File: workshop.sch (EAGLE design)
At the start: 8 parts, among them IC1 LM555N

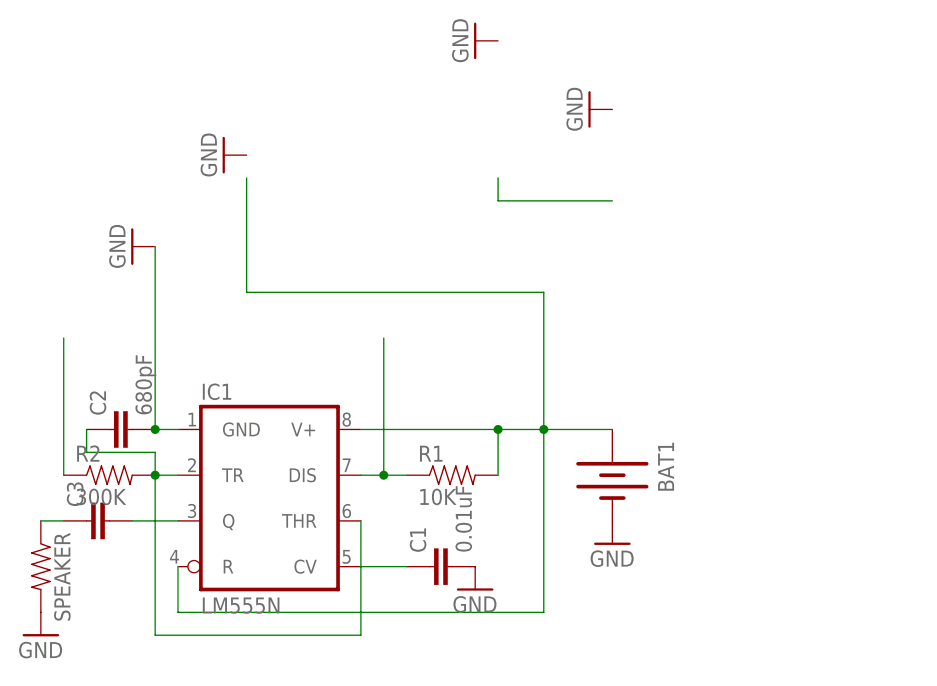
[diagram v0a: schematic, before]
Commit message: Simpler version with LED and switch
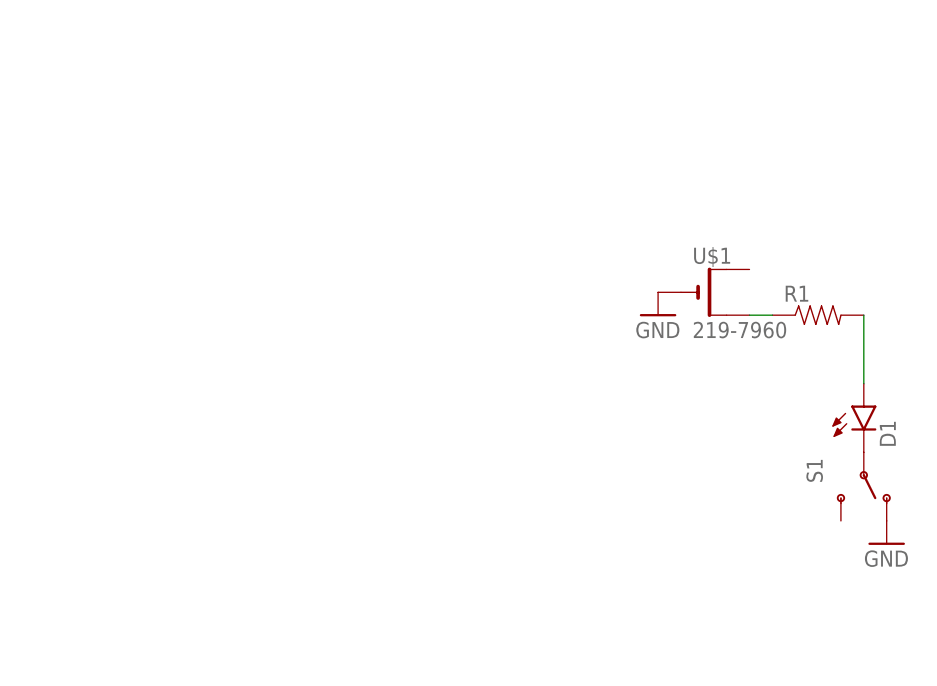
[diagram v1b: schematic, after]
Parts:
- removed BAT1: (no value), SparkFun-Electromechanical:BATTERYAAA
- removed C1: 0.01uF, SparkFun-Capacitors:CAPKIT
- removed C2: 680pF, SparkFun-Capacitors:CAPKIT
- removed C3: (no value), SparkFun-Capacitors:CAPKIT
- removed IC1: LM555N, lio:LM555N
- removed R2: 300K, SparkFun-Resistors:RESISTORKIT
- removed SPEAKER: (no value), SparkFun-Resistors:RESISTORKIT
- added D1: (no value), SparkFun-LED:LED10MM
- added S1: (no value), lio:SWITCH-SPDT
- added U$1: 219-7960, adafruit:CR2032THM
- R1: value 10K -> (none); device SparkFun-Resistors:RESISTORKIT -> SparkFun-Passives:RESISTORKIT
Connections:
- removed net COPPER: IC1.DIS, R1.1
- removed net N$21: R2.1
- removed net N$22: BAT1.+, IC1.R, IC1.V+, R1.2
- removed net N$28: C1.1, IC1.CV
- removed net N$29: C3.2, IC1.Q
- removed net N$30: C3.1, SPEAKER.1
- removed net N$31: C2.1, IC1.THR, IC1.TR, R2.2
- new net N$1: D1.A, R1.2
- new net N$2: D1.C, S1.P
- new net N$3: R1.1, U$1.+1
- net GND: now also S1.O, U$1.-; no longer BAT1.-, C1.2, C2.2, IC1.GND, SPEAKER.2
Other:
- moved on the sheet: R1
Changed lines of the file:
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@@
 </classes>
 <parts>
-<part name="BAT1" library="SparkFun-Electromechanical" deviceset="BATTERY" device="AAA"/>
-<part name="IC1" library="lio" deviceset="*555" device="N" technology="LM"/>
+<part name="GND2" library="supply1" deviceset="GND" device=""/>
+<part name="U$1" library="adafruit" deviceset="CR2032" device="THM" value="219-7960"/>
+<part name="D1" library="SparkFun-LED" deviceset="LED" device="10MM"/>
+<part name="S1" library="lio" deviceset="SWITCH-SPDT" device=""/>
 <part name="GND1" library="supply1" deviceset="GND" device=""/>
-<part name="R1" library="SparkFun-Resistors" deviceset="RESISTOR" device="KIT" value="10K"/>
-<part name="R2" library="SparkFun-Resistors" deviceset="RESISTOR" device="KIT" value="300K"/>
-<part name="C1" library="SparkFun-Capacitors" deviceset="CAP" device="KIT" value="0.01uF"/>
-<part name="C2" library="SparkFun-Capacitors" deviceset="CAP" device="KIT" value="680pF"/>
-<part name="C3" library="SparkFun-Capacitors" deviceset="CAP" device="KIT"/>
-<part name="GND2" library="supply1" deviceset="GND" device=""/>
-<part name="GND3" library="supply1" deviceset="GND" device=""/>
-<part name="SPEAKER" library="SparkFun-Resistors" deviceset="RESISTOR" device="KIT"/>
-<part name="GND4" library="supply1" deviceset="GND" device=""/>
-<part name="GND5" library="supply1" deviceset="GND" device=""/>
-<part name="GND6" library="supply1" deviceset="GND" device=""/>
-<part name="GND7" library="supply1" deviceset="GND" device=""/>
+<part name="R1" library="SparkFun-Passives" deviceset="RESISTOR" device="KIT"/>
 </parts>
 <sheets>
@@
 </plain>
 <instances>
-<instance part="BAT1" gate="G$1" x="76.2" y="60.96" rot="R270"/>
-<instance part="IC1" gate="A" x="38.1" y="58.42"/>
-<instance part="GND1" gate="1" x="22.86" y="86.36" rot="R270"/>
-<instance part="R1" gate="G$1" x="58.42" y="60.96"/>
-<instance part="R2" gate="G$1" x="20.32" y="60.96"/>
-<instance part="C1" gate="G$1" x="58.42" y="50.8" rot="R90"/>
-<instance part="C2" gate="G$1" x="22.86" y="66.04" rot="R90"/>
-<instance part="C3" gate="G$1" x="20.32" y="55.88" rot="R90"/>
-<instance part="GND2" gate="1" x="76.2" y="53.34"/>
-<instance part="GND3" gate="1" x="60.96" y="48.26"/>
-<instance part="SPEAKER" gate="G$1" x="12.7" y="50.8" rot="R270"/>
-<instance part="GND4" gate="1" x="12.7" y="43.18"/>
-<instance part="GND5" gate="1" x="73.66" y="101.6" rot="R270"/>
-<instance part="GND6" gate="1" x="33.02" y="96.52" rot="R270"/>
-<instance part="GND7" gate="1" x="60.96" y="109.22" rot="R270"/>
+<instance part="GND2" gate="1" x="81.28" y="78.74"/>
+<instance part="U$1" gate="G$1" x="86.36" y="81.28"/>
+<instance part="D1" gate="G$1" x="104.14" y="68.58"/>
+<instance part="S1" gate="1" x="104.14" y="60.96" rot="R270"/>
+<instance part="GND1" gate="1" x="106.68" y="53.34"/>
+<instance part="R1" gate="G$1" x="99.06" y="78.74"/>
 </instances>
 <busses>
@@
 <net name="GND" class="0">
 <segment>
-<pinref part="IC1" gate="A" pin="GND"/>
-<pinref part="GND1" gate="1" pin="GND"/>
-<pinref part="C2" gate="G$1" pin="2"/>
-<pinref part="C2" gate="G$1" pin="2"/>
-<wire x1="25.4" y1="86.36" x2="25.4" y2="66.04" width="0.1524" layer="91"/>
-<junction x="25.4" y="66.04"/>
-<wire x1="25.4" y1="66.04" x2="27.94" y2="66.04" width="0.1524" layer="91"/>
+<pinref part="U$1" gate="G$1" pin="-"/>
+<pinref part="GND2" gate="1" pin="GND"/>
 </segment>
 <segment>
-<pinref part="C1" gate="G$1" pin="2"/>
-<pinref part="GND3" gate="1" pin="GND"/>
-</segment>
-<segment>
-<pinref part="SPEAKER" gate="G$1" pin="2"/>
-<pinref part="GND4" gate="1" pin="GND"/>
-</segment>
-<segment>
-<pinref part="GND2" gate="1" pin="GND"/>
-<pinref part="BAT1" gate="G$1" pin="-"/>
+<pinref part="S1" gate="1" pin="O"/>
+<pinref part="GND1" gate="1" pin="GND"/>
 </segment>
 </net>
-<net name="COPPER" class="0">
+<net name="N$1" class="0">
 <segment>
-<pinref part="IC1" gate="A" pin="DIS"/>
-<pinref part="R1" gate="G$1" pin="1"/>
-<wire x1="48.26" y1="60.96" x2="50.8" y2="60.96" width="0.1524" layer="91"/>
-<wire x1="50.8" y1="60.96" x2="53.34" y2="60.96" width="0.1524" layer="91"/>
-<wire x1="50.8" y1="76.2" x2="50.8" y2="60.96" width="0.1524" layer="91"/>
-<junction x="50.8" y="60.96"/>
-</segment>
-</net>
-<net name="N$28" class="0">
-<segment>
-<pinref part="IC1" gate="A" pin="CV"/>
-<pinref part="C1" gate="G$1" pin="1"/>
-<wire x1="48.26" y1="50.8" x2="53.34" y2="50.8" width="0.1524" layer="91"/>
-</segment>
-</net>
-<net name="N$29" class="0">
-<segment>
-<pinref part="IC1" gate="A" pin="Q"/>
-<pinref part="C3" gate="G$1" pin="2"/>
-<wire x1="22.86" y1="55.88" x2="27.94" y2="55.88" width="0.1524" layer="91"/>
-</segment>
-</net>
-<net name="N$30" class="0">
-<segment>
-<pinref part="SPEAKER" gate="G$1" pin="1"/>
-<pinref part="C3" gate="G$1" pin="1"/>
-<wire x1="12.7" y1="55.88" x2="15.24" y2="55.88" width="0.1524" layer="91"/>
-</segment>
-</net>
-<net name="N$31" class="0">
-<segment>
-<pinref part="R2" gate="G$1" pin="2"/>
-<pinref part="IC1" gate="A" pin="TR"/>
-<wire x1="25.4" y1="60.96" x2="27.94" y2="60.96" width="0.1524" layer="91"/>
-<pinref part="IC1" gate="A" pin="THR"/>
-<wire x1="48.26" y1="55.88" x2="48.26" y2="43.18" width="0.1524" layer="91"/>
-<wire x1="48.26" y1="43.18" x2="25.4" y2="43.18" width="0.1524" layer="91"/>
-<wire x1="25.4" y1="43.18" x2="25.4" y2="60.96" width="0.1524" layer="91"/>
-<junction x="25.4" y="60.96"/>
-<pinref part="C2" gate="G$1" pin="1"/>
-<wire x1="17.78" y1="66.04" x2="17.78" y2="63.5" width="0.1524" layer="91"/>
-<wire x1="17.78" y1="63.5" x2="25.4" y2="63.5" width="0.1524" layer="91"/>
-<wire x1="25.4" y1="63.5" x2="25.4" y2="60.96" width="0.1524" layer="91"/>
+<wire x1="104.14" y1="78.74" x2="104.14" y2="71.12" width="0.1524" layer="91"/>
+<pinref part="D1" gate="G$1" pin="A"/>
+<pinref part="R1" gate="G$1" pin="2"/>
 </segment>
 </net>
 <net name="N$2" class="0">
 <segment>
-<wire x1="76.2" y1="91.44" x2="63.5" y2="91.44" width="0.1524" layer="91"/>
-<wire x1="63.5" y1="91.44" x2="63.5" y2="93.98" width="0.1524" layer="91"/>
+<pinref part="D1" gate="G$1" pin="C"/>
+<pinref part="S1" gate="1" pin="P"/>
 </segment>
 </net>
-<net name="N$22" class="0">
+<net name="N$3" class="0">
 <segment>
-<wire x1="35.56" y1="93.98" x2="35.56" y2="81.28" width="0.1524" layer="91"/>
-<pinref part="IC1" gate="A" pin="V+"/>
-<wire x1="48.26" y1="66.04" x2="63.5" y2="66.04" width="0.1524" layer="91"/>
-<pinref part="R1" gate="G$1" pin="2"/>
-<wire x1="63.5" y1="66.04" x2="68.58" y2="66.04" width="0.1524" layer="91"/>
-<wire x1="63.5" y1="60.96" x2="63.5" y2="66.04" width="0.1524" layer="91"/>
-<junction x="63.5" y="66.04"/>
-<pinref part="IC1" gate="A" pin="R"/>
-<wire x1="27.94" y1="50.8" x2="27.94" y2="45.72" width="0.1524" layer="91"/>
-<wire x1="27.94" y1="45.72" x2="68.58" y2="45.72" width="0.1524" layer="91"/>
-<wire x1="68.58" y1="45.72" x2="68.58" y2="66.04" width="0.1524" layer="91"/>
-<pinref part="BAT1" gate="G$1" pin="+"/>
-<wire x1="76.2" y1="66.04" x2="68.58" y2="66.04" width="0.1524" layer="91"/>
-<junction x="68.58" y="66.04"/>
-<wire x1="35.56" y1="81.28" x2="68.58" y2="81.28" width="0.1524" layer="91"/>
-<wire x1="68.58" y1="81.28" x2="68.58" y2="66.04" width="0.1524" layer="91"/>
+<pinref part="R1" gate="G$1" pin="1"/>
+<pinref part="U$1" gate="G$1" pin="+1"/>
+<wire x1="91.44" y1="78.74" x2="93.98" y2="78.74" width="0.1524" layer="91"/>
 </segment>
 </net>
-<net name="N$21" class="0">
-<segment>
-<pinref part="R2" gate="G$1" pin="1"/>
-<wire x1="15.24" y1="60.96" x2="15.24" y2="76.2" width="0.1524" layer="91"/>
-</segment>
-</net>

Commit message: Fixed switch to MHS122-1 package
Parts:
- S1: device lio:SWITCH-SPDT -> lio:SWITCH-SPDT-1
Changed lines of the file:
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@@
 <part name="U$1" library="adafruit" deviceset="CR2032" device="THM" value="219-7960"/>
 <part name="D1" library="SparkFun-LED" deviceset="LED" device="10MM"/>
-<part name="S1" library="lio" deviceset="SWITCH-SPDT" device=""/>
 <part name="GND1" library="supply1" deviceset="GND" device=""/>
 <part name="R1" library="SparkFun-Passives" deviceset="RESISTOR" device="KIT"/>
+<part name="S1" library="lio" deviceset="SWITCH-SPDT" device="-1"/>
 </parts>
 <sheets>
@@
 <instance part="U$1" gate="G$1" x="86.36" y="81.28"/>
 <instance part="D1" gate="G$1" x="104.14" y="68.58"/>
-<instance part="S1" gate="1" x="104.14" y="60.96" rot="R270"/>
 <instance part="GND1" gate="1" x="106.68" y="53.34"/>
 <instance part="R1" gate="G$1" x="99.06" y="78.74"/>
+<instance part="S1" gate="1" x="104.14" y="60.96" rot="R270"/>
 </instances>
 <busses>
@@
 </segment>
 <segment>
+<pinref part="GND1" gate="1" pin="GND"/>
 <pinref part="S1" gate="1" pin="O"/>
-<pinref part="GND1" gate="1" pin="GND"/>
 </segment>
 </net>
@@
 </segment>
 </net>
-<net name="N$2" class="0">
-<segment>
-<pinref part="D1" gate="G$1" pin="C"/>
-<pinref part="S1" gate="1" pin="P"/>
-</segment>
-</net>
 <net name="N$3" class="0">
 <segment>
@@
 </segment>
 </net>
+<net name="N$2" class="0">
+<segment>
+<pinref part="D1" gate="G$1" pin="C"/>
+<pinref part="S1" gate="1" pin="P"/>
+</segment>
+</net>
